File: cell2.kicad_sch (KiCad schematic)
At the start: 31 parts, among them K2 V23105A5001A201, Q8 IRLML0030, Q9 IRLML0030, SW4 SW_SPST, SW5 SW_SPST, U3 LMV324

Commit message: cell changes and fixes
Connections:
- net Batt+: now also C26.1, R40.2; no longer C27.1, R41.2
- net Batt-: now also C27.1, R41.2; no longer C26.1, R40.2
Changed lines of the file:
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@@
 	(hierarchical_label "Batt-"
 		(shape input)
-		(at 238.125 126.365 0)
+		(at 238.125 146.05 0)
 		(effects
 			(font
@@
 	(hierarchical_label "Batt+"
 		(shape input)
-		(at 238.125 146.05 0)
+		(at 238.125 126.365 0)
 		(effects
 			(font

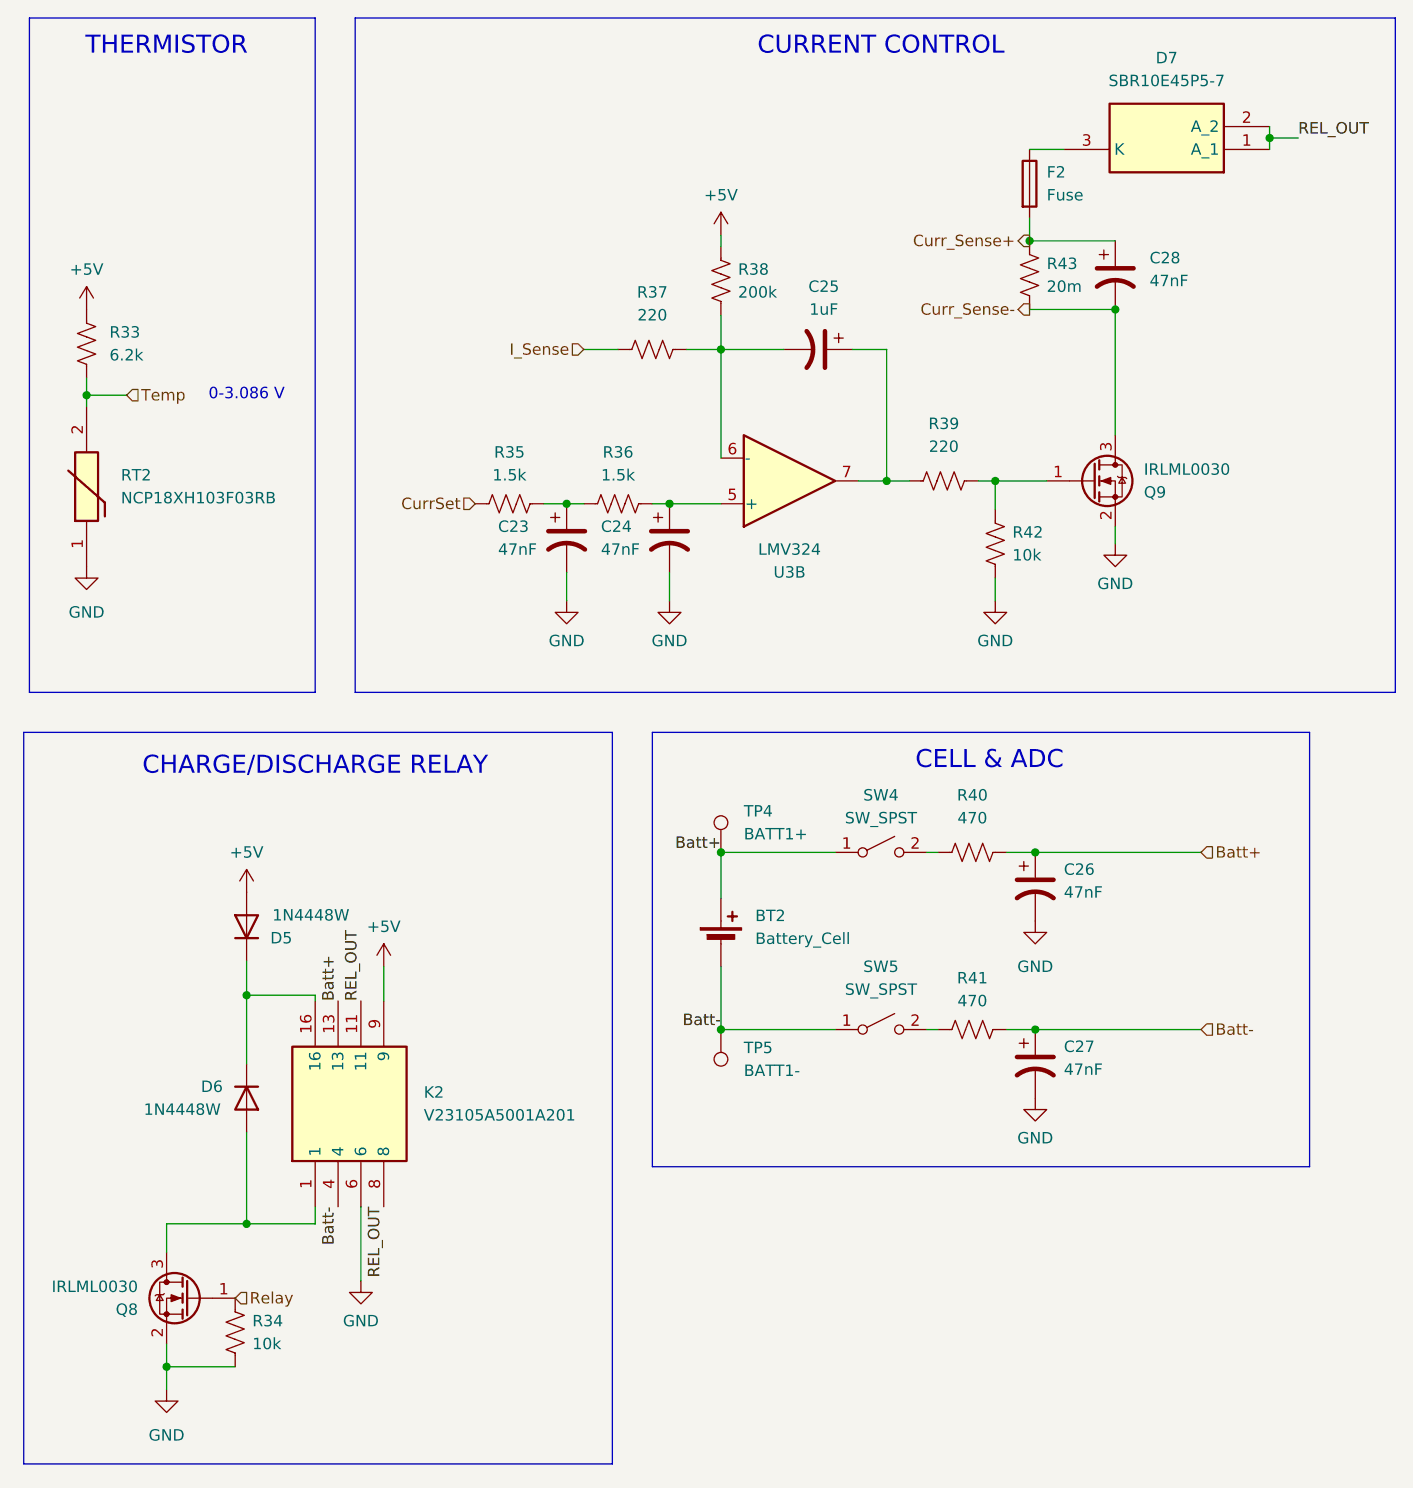
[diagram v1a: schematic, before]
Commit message: Updated current control loop hardware
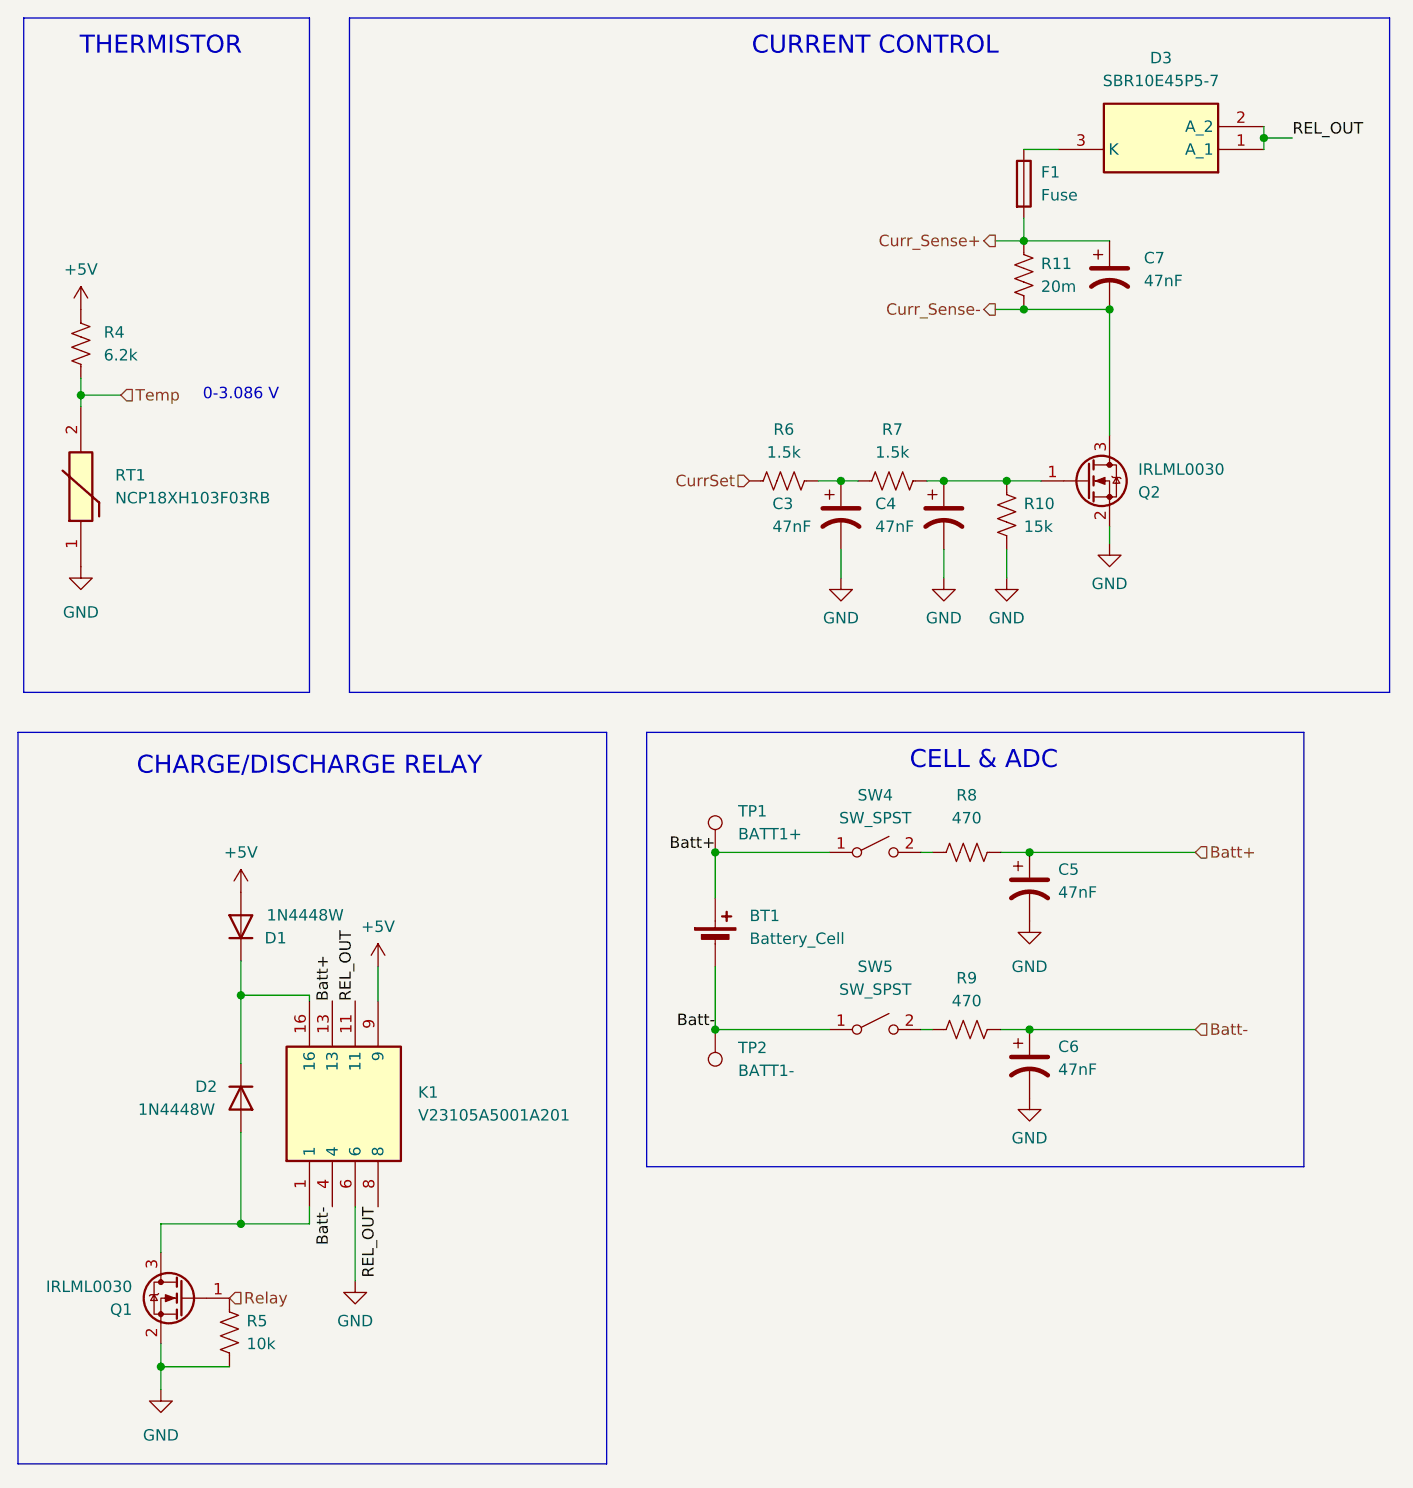
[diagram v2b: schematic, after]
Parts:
- removed BT2: Battery_Cell, symbol Device:Battery_Cell
- removed C23, C24, C26, C27, C28: 47nF, symbol Device:C_Polarized_US
- removed C25: 1uF, symbol Device:C_Polarized_US
- removed D5, D6: 1N4448W, Diode_SMD:D_SOD-123, symbol Diode:1N4448W
- removed D7: SBR10E45P5-7, SBR10E45P57, symbol SBR10E45P5-7:SBR10E45P5-7
- removed F2: Fuse, symbol Device:Fuse
- removed K2: V23105A5001A201, V23105A5001A201, symbol V23105A5001A201:V23105A5001A201
- removed Q8, Q9: IRLML0030, Package_TO_SOT_SMD:SOT-23, symbol Transistor_FET:IRLML0030
- removed R33: 6.2k, symbol Device:R_US
- removed R34, R42: 10k, symbol Device:R_US
- removed R35, R36: 1.5k, symbol Device:R_US
- removed R37, R39: 220, symbol Device:R_US
- removed R38: 200k, symbol Device:R_US
- removed R40, R41: 470, symbol Device:R_US
- removed R43: 20m, symbol Device:R_US
- removed RT2: NCP18XH103F03RB, THRMC1608X95N, symbol NCP18XH103F03RB:NCP18XH103F03RB
- removed TP4: BATT1+, symbol Connector:TestPoint
- removed TP5: BATT1-, symbol Connector:TestPoint
- removed U3: LMV324, symbol Amplifier_Operational:LMV324
- added BT1: Battery_Cell, symbol Device:Battery_Cell
- added C3, C4, C5, C6, C7: 47nF, symbol Device:C_Polarized_US
- added D1, D2: 1N4448W, Diode_SMD:D_SOD-123, symbol Diode:1N4448W
- added D3: SBR10E45P5-7, SBR10E45P57, symbol SBR10E45P5-7:SBR10E45P5-7
- added F1: Fuse, symbol Device:Fuse
- added K1: V23105A5001A201, V23105A5001A201, symbol V23105A5001A201:V23105A5001A201
- added Q1, Q2: IRLML0030, Package_TO_SOT_SMD:SOT-23, symbol Transistor_FET:IRLML0030
- added R10: 15k, symbol Device:R_US
- added R11: 20m, symbol Device:R_US
- added R4: 6.2k, symbol Device:R_US
- added R5: 10k, symbol Device:R_US
- added R6, R7: 1.5k, symbol Device:R_US
- added R8, R9: 470, symbol Device:R_US
- added RT1: NCP18XH103F03RB, THRMC1608X95N, symbol NCP18XH103F03RB:NCP18XH103F03RB
- added TP1: BATT1+, symbol Connector:TestPoint
- added TP2: BATT1-, symbol Connector:TestPoint
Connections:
- net +5V: now also D1.2 (A), K1.9, R4.1
- net Batt+: now also BT1.1 (+), C5.1, K1.13, R8.2, TP1.1
- net Batt-: now also BT1.2 (-), C6.1, K1.4, R9.2, TP2.1
- net CurrSet: now also R6.1
- net Curr_Sense+: now also C7.1, F1.2, R11.1
- net Curr_Sense-: now also C7.2, Q2.3 (D), R11.2
- net GND: now also C3.2, C4.2, C5.2, C6.2, K1.6, Q1.2 (S), Q2.2 (S), R10.1, R5.2, RT1.1
- net REL_OUT: now also D3.1 (A_1), D3.2 (A_2), K1.11, K1.8
- net Relay: now also Q1.1 (G), R5.1
- net Temp: now also R4.2, RT1.2
- net at SW5.2 (B): now also R9.1
- net at SW4.2 (B): now also R8.1
- new net: C3.1, R6.2, R7.1
- new net: C4.1, Q2.1 (G), R10.2, R7.2
- new net: D2.2 (A), K1.1, Q1.3 (D)
- new net: D1.1 (K), D2.1 (K), K1.16
- new net: D3.3 (K), F1.1

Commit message: added battery holder footprint
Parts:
- BT1: footprint (none) -> ExternalFootprints:BAT_1121
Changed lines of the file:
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@@
 	(label "Batt-"
 		(at 184.15 146.05 180)
-		(fields_autoplaced yes)
 		(effects
 			(font
@@
 	(label "REL_OUT"
 		(at 146.685 165.735 270)
-		(fields_autoplaced yes)
 		(effects
 			(font
@@
 	(label "Batt+"
 		(at 141.605 142.875 90)
-		(fields_autoplaced yes)
 		(effects
 			(font
@@
 	(label "REL_OUT"
 		(at 144.145 142.875 90)
-		(fields_autoplaced yes)
 		(effects
 			(font
@@
 	(label "Batt-"
 		(at 141.605 165.735 270)
-		(fields_autoplaced yes)
 		(effects
 			(font
@@
 	(label "Batt+"
 		(at 184.15 126.365 180)
-		(fields_autoplaced yes)
 		(effects
 			(font
@@
 	(label "REL_OUT"
 		(at 248.285 46.99 0)
-		(fields_autoplaced yes)
 		(effects
 			(font
@@
 		(shape output)
 		(at 215.265 66.04 180)
-		(fields_autoplaced yes)
 		(effects
 			(font
@@
 		(shape output)
 		(at 215.265 58.42 180)
-		(fields_autoplaced yes)
 		(effects
 			(font
@@
 		(shape input)
 		(at 187.96 85.09 180)
-		(fields_autoplaced yes)
 		(effects
 			(font
@@
 		(shape input)
 		(at 237.49 146.05 0)
-		(fields_autoplaced yes)
 		(effects
 			(font
@@
 		(shape input)
 		(at 237.49 126.365 0)
-		(fields_autoplaced yes)
 		(effects
 			(font
@@
 		(shape input)
 		(at 130.175 175.895 0)
-		(fields_autoplaced yes)
 		(effects
 			(font
@@
 		(shape input)
 		(at 118.11 75.565 0)
-		(fields_autoplaced yes)
 		(effects
 			(font
@@
 			)
 		)
-		(property "Footprint" ""
+		(property "Footprint" "ExternalFootprints:BAT_1121"
 			(at 184.15 135.001 90)
 			(effects

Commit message: All footprints assigned
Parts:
- removed SW4, SW5: SW_SPST, symbol Switch:SW_SPST
- C3, C4: value 47nF -> 0.1uF; footprint (none) -> Capacitor_SMD:C_0805_2012Metric
- C5, C6, C7: footprint (none) -> Capacitor_SMD:C_0805_2012Metric
- F1: footprint (none) -> Fuse:Fuse_1812_4532Metric
- R10: value 15k -> 470; footprint (none) -> Resistor_SMD:R_0805_2012Metric
- R11: value 20m -> 470; footprint (none) -> Resistor_SMD:R_0805_2012Metric
- R4, R5, R6, R7: footprint (none) -> Resistor_SMD:R_0805_2012Metric
- R8: value 470 -> 15k; footprint (none) -> Resistor_SMD:R_0805_2012Metric
- R9: value 470 -> 20m; footprint (none) -> Resistor_SMD:R_1206_3216Metric
- TP1, TP2: footprint (none) -> UTSVT_Special:TestPoint_HEX_3mmID
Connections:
- net Batt+: now also C6.1, R10.1, R10.2; no longer C5.1, R8.2
- net Batt-: now also C7.1, R11.1, R11.2; no longer C6.1, R9.2
- net Curr_Sense+: now also C5.1, R9.1; no longer C7.1, R11.1
- net Curr_Sense-: now also C5.2, R9.2; no longer C7.2, R11.2
- net GND: now also C7.2, R8.1; no longer C5.2, R10.1
- net at C4.1, Q2.1 (G), R7.2: now also R8.2; no longer R10.2
